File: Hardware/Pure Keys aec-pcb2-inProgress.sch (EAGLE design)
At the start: 56 parts, among them IC1 TL074P, IC5 TL074P, Q2 20MHz, T1 2N3904, U2 LM4040A50IDBZT, U3 328P

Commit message: updated in progress board added text layer text added classes for power rerouted
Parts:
- U2: value LM4040A50IDBZT -> LM4040
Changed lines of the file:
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@@
 <class number="0" name="default" width="0" drill="0">
+</class>
+<class number="1" name="Power" width="0.8" drill="0">
 </class>
 </classes>
@@
 <part name="CLK_IN" library="GMSN" deviceset="PJ302M" device="" value="PJ302M"/>
 <part name="GND13" library="supply1" library_urn="urn:adsk.eagle:library:371" deviceset="GND" device=""/>
-<part name="U2" library="GMSN" deviceset="LM4040A50IDBZT" device=""/>
+<part name="U2" library="GMSN" deviceset="LM4040A50IDBZT" device="" value="LM4040"/>
 <part name="R3" library="rcl" deviceset="R-US_" device="R0805" value="10K"/>
 <part name="V1" library="74ttl-din" library_urn="urn:adsk.eagle:library:84" deviceset="74*238" device="N" package3d_urn="urn:adsk.eagle:package:1462/1"/>
@@
 </busses>
 <nets>
-<net name="GND" class="0">
+<net name="GND" class="1">
 <segment>
 <pinref part="ISP1" gate="G$1" pin="GND"/>
@@
 </segment>
 </net>
-<net name="5V" class="0">
+<net name="5V" class="1">
 <segment>
 <pinref part="ISP1" gate="G$1" pin="VCC"/>
@@
 </busses>
 <nets>
-<net name="5V" class="0">
+<net name="5V" class="1">
 <segment>
 <pinref part="JP2" gate="G$1" pin="VBUS"/>
@@
 </segment>
 </net>
-<net name="GND" class="0">
+<net name="GND" class="1">
 <segment>
 <pinref part="JP2" gate="G$1" pin="GND"/>
@@
 </segment>
 </net>
-<net name="GND" class="0">
+<net name="GND" class="1">
 <segment>
 <pinref part="R18" gate="G$1" pin="1"/>
@@
 </busses>
 <nets>
-<net name="GND" class="0">
+<net name="GND" class="1">
 <segment>
 <pinref part="IC1" gate="P" pin="V-"/>
@@
 </segment>
 </net>
-<net name="5V" class="0">
+<net name="5V" class="1">
 <segment>
 <pinref part="C3" gate="G$1" pin="1"/>
@@
 </segment>
 </net>
-<net name="5V" class="0">
+<net name="5V" class="1">
 <segment>
 <pinref part="C6" gate="G$1" pin="1"/>
@@
 </segment>
 </net>
-<net name="GND" class="0">
+<net name="GND" class="1">
 <segment>
 <pinref part="CV4" gate="G$1" pin="SLEEVE"/>
@@
 </segment>
 </net>
-<net name="GND" class="0">
+<net name="GND" class="1">
 <segment>
 <pinref part="GLIDE1" gate="G$1" pin="3"/>
@@
 </segment>
 </net>
-<net name="5V" class="0">
+<net name="5V" class="1">
 <segment>
 <pinref part="GLIDE1" gate="G$1" pin="1"/>
@@
 </busses>
 <nets>
-<net name="GND" class="0">
+<net name="GND" class="1">
 <segment>
 <pinref part="T1" gate="G$1" pin="E"/>
@@
 </segment>
 </net>
-<net name="5V" class="0">
+<net name="5V" class="1">
 <segment>
 <pinref part="R5" gate="G$1" pin="2"/>

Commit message: updated board and tests
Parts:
- IC1, IC5: value TL074P -> MCP6004P; device GMSN:TL074P -> GMSN-R2Project:MCP6004P
- U$4: value M10X22X10_LOCK -> KeyBoard Connector
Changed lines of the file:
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@@
 <part name="R21" library="rcl" deviceset="R-US_" device="R0805" value="10K"/>
 <part name="R22" library="rcl" deviceset="R-US_" device="R0805" value="10K"/>
-<part name="U$4" library="SparkFun-Connectors" deviceset="M10X2" device="2X10_LOCK"/>
+<part name="U$4" library="SparkFun-Connectors" deviceset="M10X2" device="2X10_LOCK" value="KeyBoard Connector"/>
 <part name="TRIG2" library="GMSN" deviceset="PJ302M" device="" value="PJ302M"/>
 <part name="TRIG3" library="GMSN" deviceset="PJ302M" device="" value="PJ302M"/>
 <part name="TRIG4" library="GMSN" deviceset="PJ302M" device="" value="PJ302M"/>
-<part name="IC5" library="GMSN" deviceset="TL074" device="P" value="TL074P"/>
+<part name="IC5" library="GMSN-R2Project" deviceset="MCP6004" device="P" value="MCP6004P"/>
 <part name="CV2" library="GMSN" deviceset="PJ302M" device="" value="PJ302M"/>
 <part name="CV3" library="GMSN" deviceset="PJ302M" device="" value="PJ302M"/>
@@
 <part name="C11" library="rcl" deviceset="C-US" device="C0805K" value="100n"/>
 <part name="JP2" library="SparkFun-Connectors" deviceset="USB" device="PTH" value="USB-B"/>
-<part name="IC1" library="GMSN" deviceset="TL074" device="P" value="TL074P"/>
+<part name="IC1" library="GMSN-R2Project" deviceset="MCP6004" device="P" value="MCP6004P"/>
 <part name="C3" library="rcl" deviceset="C-US" device="C0805K" value="100n"/>
 <part name="C5" library="rcl" deviceset="C-US" device="C0805K" value="100n"/>

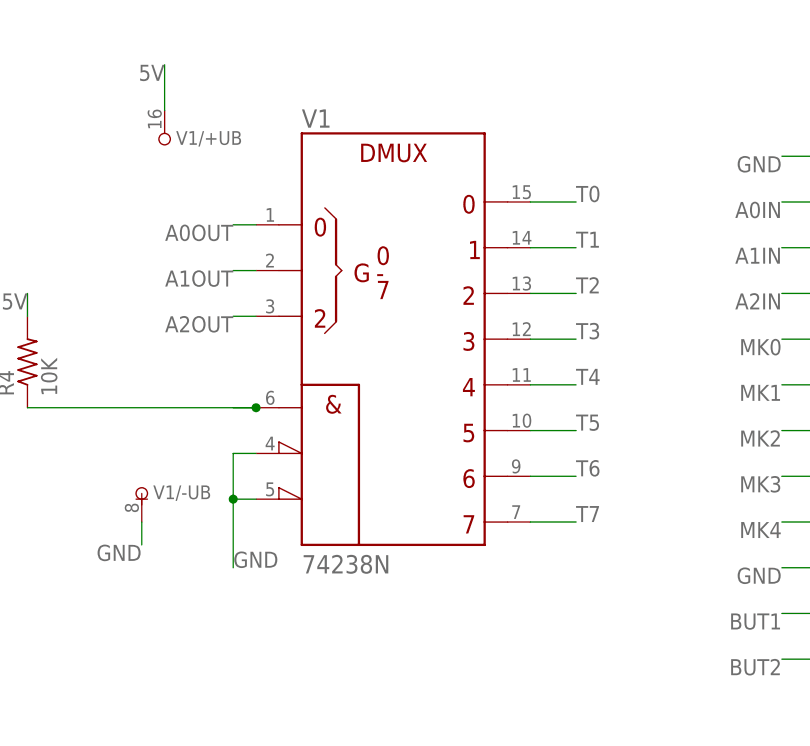
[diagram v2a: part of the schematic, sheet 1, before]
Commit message: changed 74238 for 74138
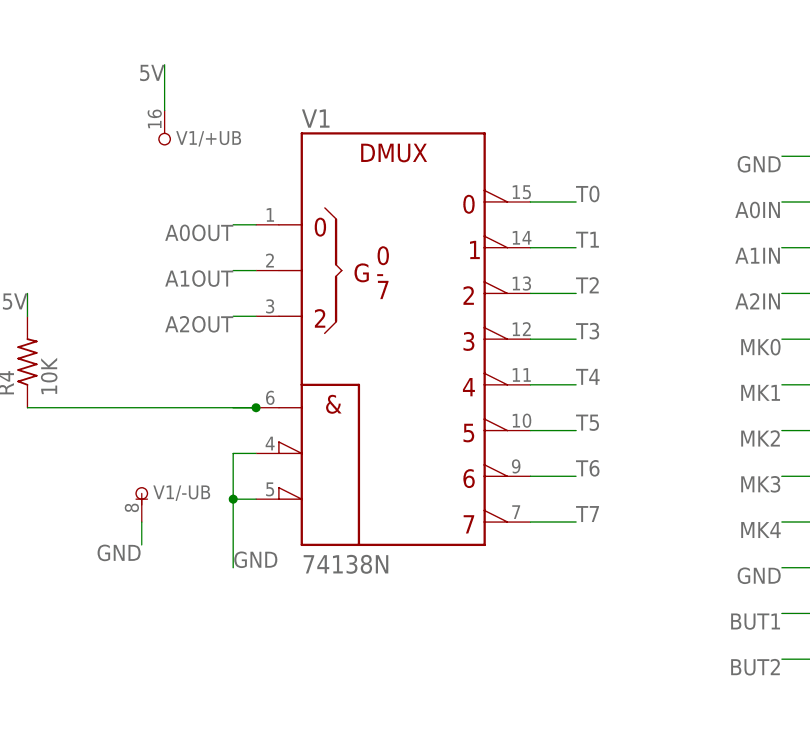
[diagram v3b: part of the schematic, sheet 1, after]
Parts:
- V1: value 74238N -> 74138N; device 74ttl-din:74238N -> 74ttl-din:74138N
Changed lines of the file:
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@@
 <part name="U2" library="GMSN" deviceset="LM4040A50IDBZT" device="" value="LM4040"/>
 <part name="R3" library="rcl" deviceset="R-US_" device="R0805" value="10K"/>
-<part name="V1" library="74ttl-din" library_urn="urn:adsk.eagle:library:84" deviceset="74*238" device="N" package3d_urn="urn:adsk.eagle:package:1462/1"/>
+<part name="V1" library="74ttl-din" library_urn="urn:adsk.eagle:library:84" deviceset="74*138" device="N" package3d_urn="urn:adsk.eagle:package:1462/1"/>
 <part name="V2" library="74ttl-din" library_urn="urn:adsk.eagle:library:84" deviceset="74*151" device="N" package3d_urn="urn:adsk.eagle:package:1462/1"/>
 <part name="U3" library="SparkFun-IC-Microcontroller" deviceset="ATMEGA328P_PDIP" device="" value="328P"/>

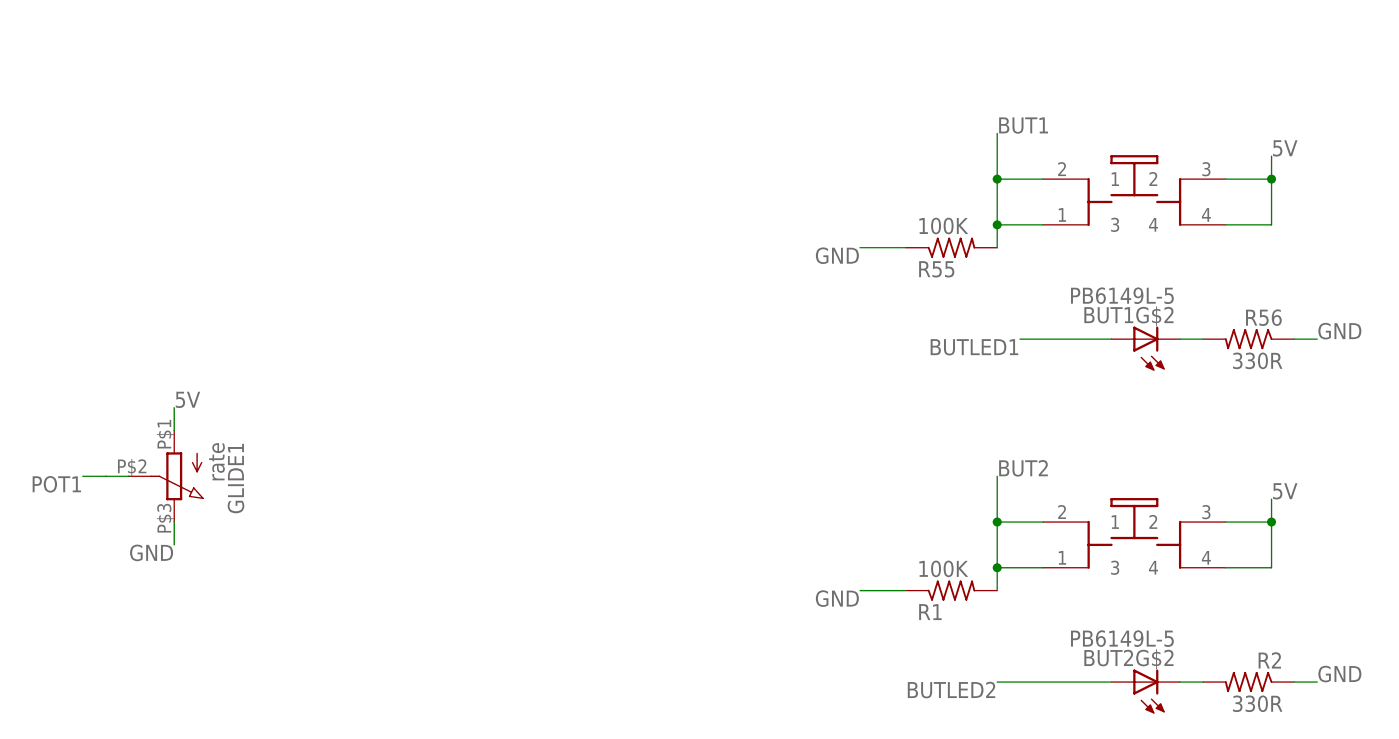
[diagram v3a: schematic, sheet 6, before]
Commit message: updated switches on in progress
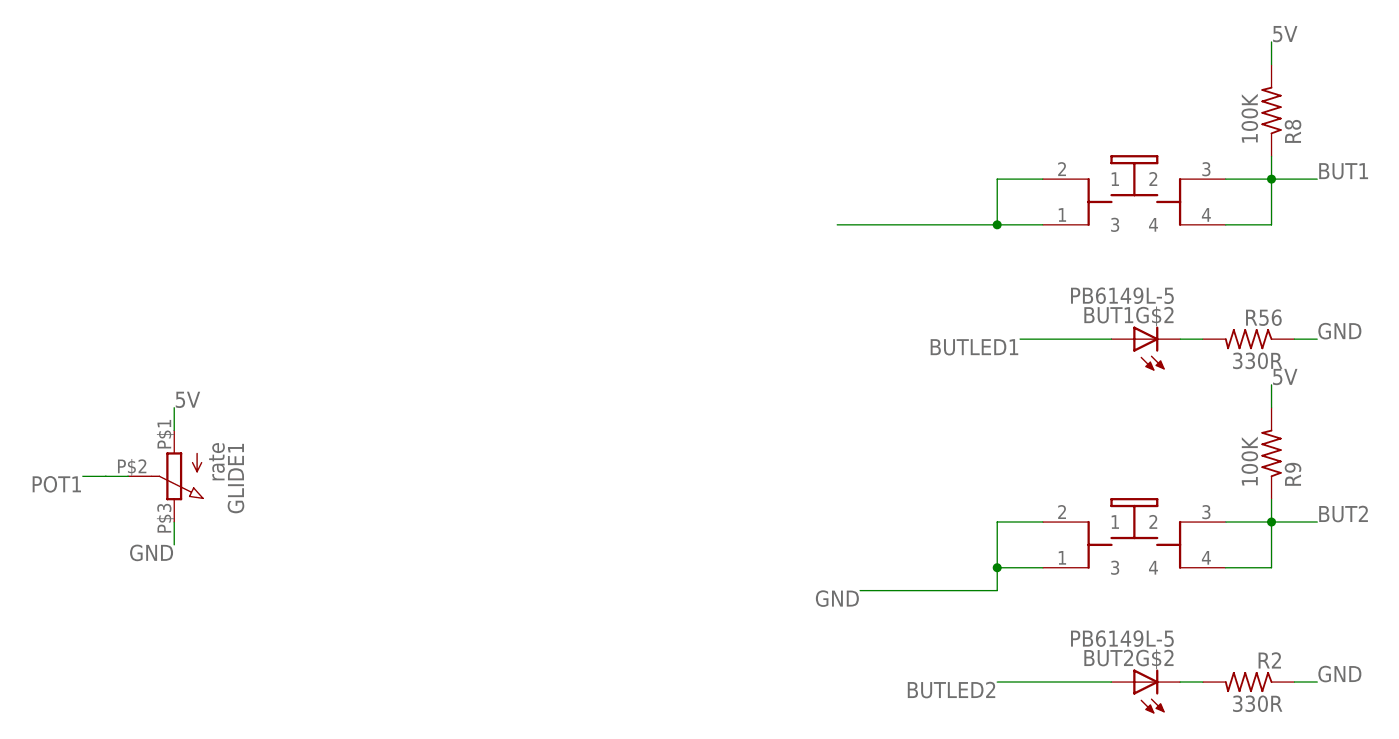
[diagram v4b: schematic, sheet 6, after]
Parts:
- removed R1, R55: 100K, rcl:R-US_R0805
- added R8, R9: 100K, rcl:R-US_R0805
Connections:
- net 5V: now also R8.2, R9.2; no longer BUT1G$1.2, BUT1G$1.4, BUT2G$1.2, BUT2G$1.4
- net BUT1: now also BUT1G$1.2, BUT1G$1.4, R8.1; no longer BUT1G$1.1, BUT1G$1.3, R55.2
- net BUT2: now also BUT2G$1.2, BUT2G$1.4, R9.1; no longer BUT2G$1.1, BUT2G$1.3, R1.2
- net GND: now also BUT1G$1.1, BUT1G$1.3, BUT2G$1.1, BUT2G$1.3; no longer R1.1, R55.1
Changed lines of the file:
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@@
 <?xml version="1.0" encoding="utf-8"?>
 <!DOCTYPE eagle SYSTEM "eagle.dtd">
-<eagle version="8.6.0">
+<eagle version="8.7.0">
 <drawing>
 <settings>
@@
 <part name="GLIDE1" library="GMSN" deviceset="9MMPOT" device="" value="rate"/>
 <part name="BUT1" library="INSTRUO" deviceset="PB6149L-5" device=""/>
-<part name="R55" library="rcl" deviceset="R-US_" device="R0805" value="100K"/>
 <part name="R56" library="rcl" deviceset="R-US_" device="R0805" value="330R"/>
 <part name="BUT2" library="INSTRUO" deviceset="PB6149L-5" device=""/>
-<part name="R1" library="rcl" deviceset="R-US_" device="R0805" value="100K"/>
 <part name="R2" library="rcl" deviceset="R-US_" device="R0805" value="330R"/>
 <part name="T1" library="INSTRUO" deviceset="TRANSISTOR_MMBT3904" device="" value="2N3904"/>
@@
 <part name="C18" library="rcl" deviceset="C-US" device="C0805K" value="22p"/>
 <part name="R4" library="rcl" deviceset="R-US_" device="R0805" value="10K"/>
+<part name="R8" library="rcl" deviceset="R-US_" device="R0805" value="100K"/>
+<part name="R9" library="rcl" deviceset="R-US_" device="R0805" value="100K"/>
 </parts>
 <sheets>
@@
 <instance part="BUT1" gate="G$1" x="119.38" y="68.58"/>
 <instance part="BUT1" gate="G$2" x="119.38" y="50.8" rot="R90"/>
-<instance part="R55" gate="G$1" x="99.06" y="60.96" rot="MR180"/>
 <instance part="R56" gate="G$1" x="132.08" y="50.8" rot="MR0"/>
 <instance part="BUT2" gate="G$1" x="119.38" y="30.48"/>
 <instance part="BUT2" gate="G$2" x="119.38" y="12.7" rot="R90"/>
-<instance part="R1" gate="G$1" x="99.06" y="22.86" rot="MR180"/>
 <instance part="R2" gate="G$1" x="132.08" y="12.7" rot="MR0"/>
+<instance part="R8" gate="G$1" x="134.62" y="76.2" rot="MR90"/>
+<instance part="R9" gate="G$1" x="134.62" y="38.1" rot="MR90"/>
 </instances>
 <busses>
@@
 </segment>
 <segment>
-<pinref part="R55" gate="G$1" pin="1"/>
-<wire x1="93.98" y1="60.96" x2="88.9" y2="60.96" width="0.1524" layer="91"/>
-<label x="88.9" y="60.96" size="1.778" layer="95" rot="R180"/>
-</segment>
-<segment>
 <pinref part="R2" gate="G$1" pin="1"/>
 <wire x1="137.16" y1="12.7" x2="139.7" y2="12.7" width="0.1524" layer="91"/>
@@
 </segment>
 <segment>
-<pinref part="R1" gate="G$1" pin="1"/>
-<wire x1="93.98" y1="22.86" x2="88.9" y2="22.86" width="0.1524" layer="91"/>
 <label x="88.9" y="22.86" size="1.778" layer="95" rot="R180"/>
+<pinref part="BUT2" gate="G$1" pin="3"/>
+<wire x1="109.22" y1="25.4" x2="104.14" y2="25.4" width="0.1524" layer="91"/>
+<wire x1="104.14" y1="25.4" x2="104.14" y2="22.86" width="0.1524" layer="91"/>
+<pinref part="BUT2" gate="G$1" pin="1"/>
+<wire x1="109.22" y1="30.48" x2="104.14" y2="30.48" width="0.1524" layer="91"/>
+<wire x1="104.14" y1="30.48" x2="104.14" y2="25.4" width="0.1524" layer="91"/>
+<junction x="104.14" y="25.4"/>
+<wire x1="88.9" y1="22.86" x2="104.14" y2="22.86" width="0.1524" layer="91"/>
+</segment>
+<segment>
+<pinref part="BUT1" gate="G$1" pin="1"/>
+<wire x1="109.22" y1="68.58" x2="104.14" y2="68.58" width="0.1524" layer="91"/>
+<wire x1="104.14" y1="68.58" x2="104.14" y2="63.5" width="0.1524" layer="91"/>
+<pinref part="BUT1" gate="G$1" pin="3"/>
+<wire x1="104.14" y1="63.5" x2="109.22" y2="63.5" width="0.1524" layer="91"/>
+<wire x1="104.14" y1="63.5" x2="86.36" y2="63.5" width="0.1524" layer="91"/>
+<junction x="104.14" y="63.5"/>
 </segment>
 </net>
@@
 <label x="12.7" y="43.18" size="1.778" layer="95"/>
 </segment>
+<segment>
+<pinref part="R8" gate="G$1" pin="2"/>
+<wire x1="134.62" y1="81.28" x2="134.62" y2="83.82" width="0.1524" layer="91"/>
+<label x="134.62" y="83.82" size="1.778" layer="95"/>
+</segment>
+<segment>
+<pinref part="R9" gate="G$1" pin="2"/>
+<wire x1="134.62" y1="45.72" x2="134.62" y2="43.18" width="0.1524" layer="91"/>
+<label x="134.62" y="45.72" size="1.778" layer="95"/>
+</segment>
+</net>
+<net name="BUTLED1" class="0">
+<segment>
+<pinref part="BUT1" gate="G$2" pin="A"/>
+<wire x1="106.68" y1="50.8" x2="116.84" y2="50.8" width="0.1524" layer="91"/>
+<label x="106.68" y="50.8" size="1.778" layer="95" rot="R180"/>
+</segment>
+</net>
+<net name="N$65" class="0">
+<segment>
+<pinref part="BUT1" gate="G$2" pin="C"/>
+<pinref part="R56" gate="G$1" pin="2"/>
+<wire x1="127" y1="50.8" x2="124.46" y2="50.8" width="0.1524" layer="91"/>
+</segment>
+</net>
+<net name="N$8" class="0">
+<segment>
+<pinref part="BUT2" gate="G$2" pin="C"/>
+<pinref part="R2" gate="G$1" pin="2"/>
+<wire x1="127" y1="12.7" x2="124.46" y2="12.7" width="0.1524" layer="91"/>
+</segment>
+</net>
+<net name="BUTLED2" class="0">
+<segment>
+<pinref part="BUT2" gate="G$2" pin="A"/>
+<wire x1="116.84" y1="12.7" x2="104.14" y2="12.7" width="0.1524" layer="91"/>
+<label x="104.14" y="12.7" size="1.778" layer="95" rot="R180"/>
+</segment>
+</net>
+<net name="BUT1" class="0">
 <segment>
 <pinref part="BUT1" gate="G$1" pin="2"/>
@@
 <wire x1="134.62" y1="63.5" x2="134.62" y2="68.58" width="0.1524" layer="91"/>
 <junction x="134.62" y="68.58"/>
-<label x="134.62" y="71.12" size="1.778" layer="95"/>
-</segment>
+<pinref part="R8" gate="G$1" pin="1"/>
+<wire x1="134.62" y1="68.58" x2="139.7" y2="68.58" width="0.1524" layer="91"/>
+<label x="139.7" y="68.58" size="1.778" layer="95"/>
+</segment>
+</net>
+<net name="BUT2" class="0">
 <segment>
 <pinref part="BUT2" gate="G$1" pin="2"/>
@@
 <wire x1="134.62" y1="25.4" x2="134.62" y2="30.48" width="0.1524" layer="91"/>
 <junction x="134.62" y="30.48"/>
-<label x="134.62" y="33.02" size="1.778" layer="95"/>
-</segment>
-</net>
-<net name="BUT1" class="0">
-<segment>
-<pinref part="BUT1" gate="G$1" pin="1"/>
-<wire x1="109.22" y1="68.58" x2="104.14" y2="68.58" width="0.1524" layer="91"/>
-<pinref part="BUT1" gate="G$1" pin="3"/>
-<wire x1="109.22" y1="63.5" x2="104.14" y2="63.5" width="0.1524" layer="91"/>
-<wire x1="104.14" y1="63.5" x2="104.14" y2="68.58" width="0.1524" layer="91"/>
-<pinref part="R55" gate="G$1" pin="2"/>
-<wire x1="104.14" y1="63.5" x2="104.14" y2="60.96" width="0.1524" layer="91"/>
-<junction x="104.14" y="63.5"/>
-<wire x1="104.14" y1="68.58" x2="104.14" y2="73.66" width="0.1524" layer="91"/>
-<junction x="104.14" y="68.58"/>
-<label x="104.14" y="73.66" size="1.778" layer="95"/>
-</segment>
-</net>
-<net name="BUTLED1" class="0">
-<segment>
-<pinref part="BUT1" gate="G$2" pin="A"/>
-<wire x1="106.68" y1="50.8" x2="116.84" y2="50.8" width="0.1524" layer="91"/>
-<label x="106.68" y="50.8" size="1.778" layer="95" rot="R180"/>
-</segment>
-</net>
-<net name="N$65" class="0">
-<segment>
-<pinref part="BUT1" gate="G$2" pin="C"/>
-<pinref part="R56" gate="G$1" pin="2"/>
-<wire x1="127" y1="50.8" x2="124.46" y2="50.8" width="0.1524" layer="91"/>
-</segment>
-</net>
-<net name="N$8" class="0">
-<segment>
-<pinref part="BUT2" gate="G$2" pin="C"/>
-<pinref part="R2" gate="G$1" pin="2"/>
-<wire x1="127" y1="12.7" x2="124.46" y2="12.7" width="0.1524" layer="91"/>
-</segment>
-</net>
-<net name="BUT2" class="0">
-<segment>
-<pinref part="BUT2" gate="G$1" pin="3"/>
-<wire x1="109.22" y1="25.4" x2="104.14" y2="25.4" width="0.1524" layer="91"/>
-<pinref part="R1" gate="G$1" pin="2"/>
-<wire x1="104.14" y1="25.4" x2="104.14" y2="22.86" width="0.1524" layer="91"/>
-<pinref part="BUT2" gate="G$1" pin="1"/>
-<wire x1="109.22" y1="30.48" x2="104.14" y2="30.48" width="0.1524" layer="91"/>
-<wire x1="104.14" y1="30.48" x2="104.14" y2="25.4" width="0.1524" layer="91"/>
-<junction x="104.14" y="25.4"/>
-<wire x1="104.14" y1="30.48" x2="104.14" y2="35.56" width="0.1524" layer="91"/>
-<junction x="104.14" y="30.48"/>
-<label x="104.14" y="35.56" size="1.778" layer="95"/>
-</segment>
-</net>
-<net name="BUTLED2" class="0">
-<segment>
-<pinref part="BUT2" gate="G$2" pin="A"/>
-<wire x1="116.84" y1="12.7" x2="104.14" y2="12.7" width="0.1524" layer="91"/>
-<label x="104.14" y="12.7" size="1.778" layer="95" rot="R180"/>
-</segment>
-</net>
+<pinref part="R9" gate="G$1" pin="1"/>
+<wire x1="134.62" y1="30.48" x2="139.7" y2="30.48" width="0.1524" layer="91"/>
+<label x="139.7" y="30.48" size="1.778" layer="95"/>
+</segment>
+</net>
